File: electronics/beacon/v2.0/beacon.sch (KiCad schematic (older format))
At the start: 15 parts, among them J1 L, J2 R, J3 TPI, Q1 BSS138, U1 ATTINY10-TS, U2 MIC5225-1.8YM5

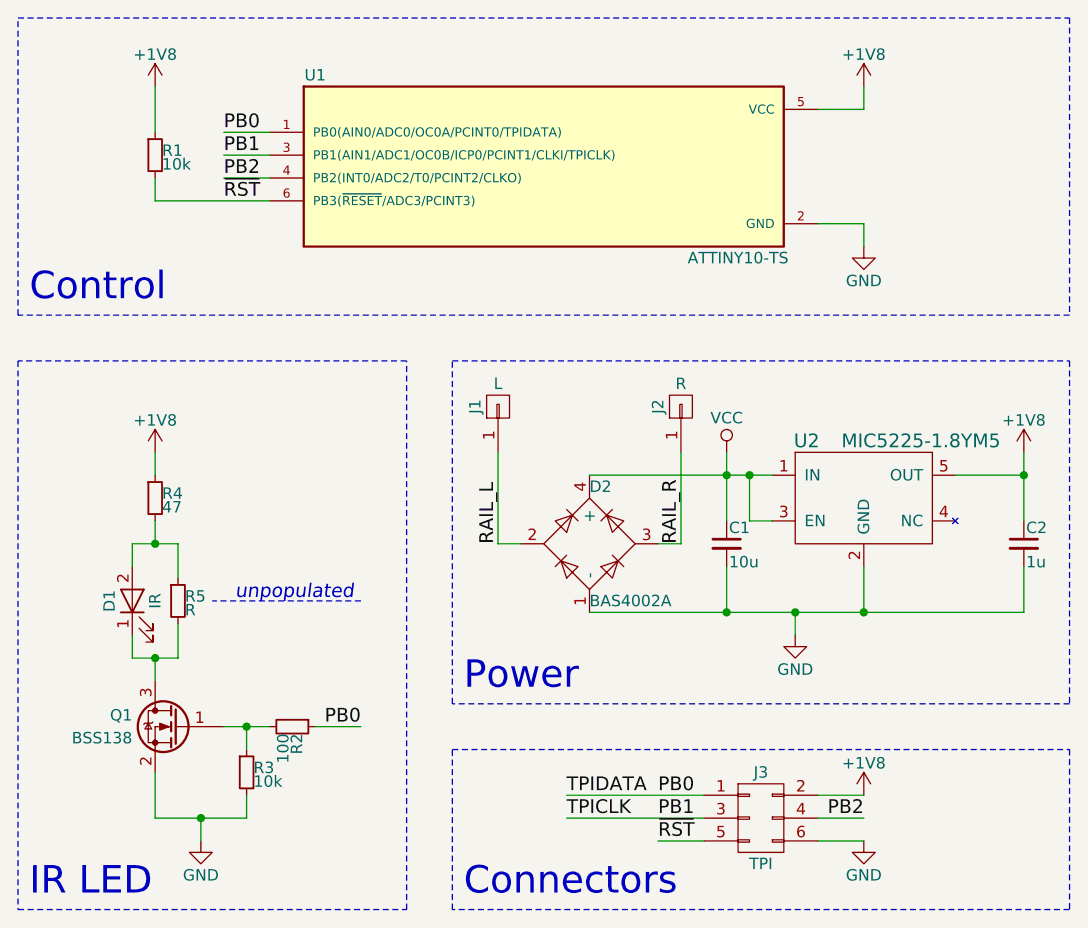
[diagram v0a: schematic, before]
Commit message: electronics: beacon: Add solder jumper to v2.0
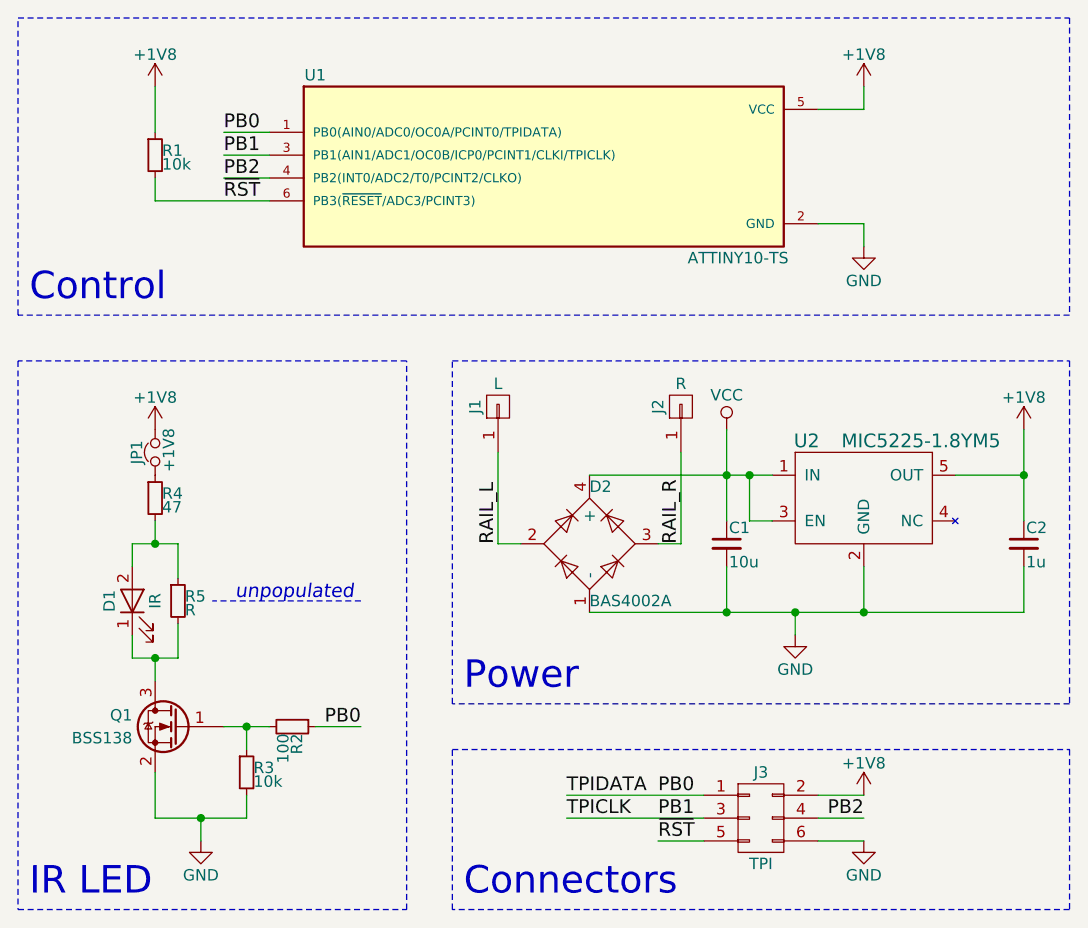
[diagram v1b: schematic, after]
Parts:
- added JP1: +1V8, bcan:Solder_Jumper_NC_Small, symbol Jumper_NC_Small
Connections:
- net +1V8: now also JP1.2; no longer R4.1
- new net: JP1.1, R4.1
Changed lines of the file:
@@
 Sheet 1 1
 Title "IR Beacon Board"
-Date "2017-03-21"
+Date "2017-05-02"
 Rev "2.0"
 Comp "ECE 445"
@@
 L VCC #PWR04
 U 1 1 58D18C7E
-P 6700 4200
-F 0 "#PWR04" H 6700 4050 50  0001 C CNN
-F 1 "VCC" H 6700 4350 50  0000 C CNN
-F 2 "" H 6700 4200 50  0001 C CNN
-F 3 "" H 6700 4200 50  0001 C CNN
-	1    6700 4200
+P 6700 4100
+F 0 "#PWR04" H 6700 3950 50  0001 C CNN
+F 1 "VCC" H 6700 4250 50  0000 C CNN
+F 2 "" H 6700 4100 50  0001 C CNN
+F 3 "" H 6700 4100 50  0001 C CNN
+	1    6700 4100
 	1    0    0    -1
 $EndComp
@@
 Connection ~ 8000 4300
 Wire Wire Line
-	8000 4200 8000 4500
+	8000 4100 8000 4300
+Wire Wire Line
+	8000 4300 8000 4500
 Connection ~ 4600 5400
 Connection ~ 4400 5800
@@
 	4400 5800 4400 5900
 Wire Wire Line
-	4200 5800 4600 5800
+	4200 5800 4400 5800
+Wire Wire Line
+	4400 5800 4600 5800
 Wire Wire Line
 	4600 5800 4600 5700
@@
 	4600 5400 4600 5500
 Wire Wire Line
-	4500 5400 4700 5400
+	4500 5400 4600 5400
+Wire Wire Line
+	4600 5400 4700 5400
 Wire Wire Line
 	4200 2800 4200 2600
@@
 	4200 5100 4200 5200
 Wire Wire Line
-	4100 5100 4300 5100
-Wire Wire Line
-	4200 4300 4200 4200
+	4100 5100 4200 5100
+Wire Wire Line
+	4200 5100 4300 5100
 Connection ~ 4200 4600
 Wire Wire Line
@@
 	4300 4600 4300 4750
 Wire Wire Line
-	4100 4600 4300 4600
+	4100 4600 4200 4600
+Wire Wire Line
+	4200 4600 4300 4600
 Wire Wire Line
 	4100 4700 4100 4600
@@
 Connection ~ 7300 4900
 Wire Wire Line
-	6100 4900 8000 4900
+	6100 4900 6700 4900
+Wire Wire Line
+	6700 4900 7000 4900
+Wire Wire Line
+	7000 4900 7300 4900
+Wire Wire Line
+	7300 4900 8000 4900
 Wire Wire Line
 	4900 5400 5100 5400
@@
 	8200 3600 3600 3600
 Wire Wire Line
-	6100 4300 6900 4300
-Wire Wire Line
-	6700 4200 6700 4500
+	6100 4300 6700 4300
+Wire Wire Line
+	6700 4300 6800 4300
+Wire Wire Line
+	6800 4300 6900 4300
+Wire Wire Line
+	6700 4100 6700 4300
+Wire Wire Line
+	6700 4300 6700 4500
 Connection ~ 6700 4300
 Wire Wire Line
@@
 L +1V8 #PWR06
 U 1 1 59018E39
-P 4200 4200
-F 0 "#PWR06" H 4200 4050 50  0001 C CNN
-F 1 "+1V8" H 4200 4340 50  0000 C CNN
-F 2 "" H 4200 4200 50  0001 C CNN
-F 3 "" H 4200 4200 50  0001 C CNN
-	1    4200 4200
+P 4200 4100
+F 0 "#PWR06" H 4200 3950 50  0001 C CNN
+F 1 "+1V8" H 4200 4240 50  0000 C CNN
+F 2 "" H 4200 4100 50  0001 C CNN
+F 3 "" H 4200 4100 50  0001 C CNN
+	1    4200 4100
 	1    0    0    -1
 $EndComp
@@
 L +1V8 #PWR07
 U 1 1 59018E74
-P 8000 4200
-F 0 "#PWR07" H 8000 4050 50  0001 C CNN
-F 1 "+1V8" H 8000 4340 50  0000 C CNN
-F 2 "" H 8000 4200 50  0001 C CNN
-F 3 "" H 8000 4200 50  0001 C CNN
-	1    8000 4200
+P 8000 4100
+F 0 "#PWR07" H 8000 3950 50  0001 C CNN
+F 1 "+1V8" H 8000 4240 50  0000 C CNN
+F 2 "" H 8000 4100 50  0001 C CNN
+F 3 "" H 8000 4100 50  0001 C CNN
+	1    8000 4100
 	1    0    0    -1
 $EndComp
@@
 Text Label 6400 5800 0    60   ~ 0
 PB1
+$Comp
+L Jumper_NC_Small JP1
+U 1 1 5903146F
+P 4200 4200
+F 0 "JP1" H 4200 4280 50  0000 C CNN
+F 1 "+1V8" H 4210 4140 50  0000 C CNN
+F 2 "bcan:Solder_Jumper_NC_Small" H 4200 4200 50  0001 C CNN
+F 3 "" H 4200 4200 50  0001 C CNN
+	1    4200 4200
+	0    -1   -1   0
+$EndComp
 $EndSCHEMATC
